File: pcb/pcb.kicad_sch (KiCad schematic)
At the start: 30 parts, among them J1 Barrel_Jack_Switch, Q1 RQ5P010SN, SW1 SW_SPST, SW2 SW_SPST, SW3 SW_SPST, U1 L7805, U2 MCP1406/07, U3 MCP7940N-xSN, U4 Pico, Y1 Crystal

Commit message: finished routing
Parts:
- removed Y1: Crystal, vfd:Crystal_DS26_D2.0mm_L6.0mm_Horizontal_SMT, symbol Device:Crystal
- added C10, C9: 0.1uF, Capacitor_SMD:C_1206_3216Metric_Pad1.33x1.80mm_HandSolder, symbol Device:C
- added H1: MountingHole_Pad, MountingHole:MountingHole_3.2mm_M3_DIN965_Pad, symbol Mechanical:MountingHole_Pad
- added J2: Conn_01x05_Pin, Connector_PinHeader_2.54mm:PinHeader_1x05_P2.54mm_Vertical, symbol Connector:Conn_01x05_Pin
- added J3: Conn_01x03_Pin, Connector_PinHeader_2.54mm:PinHeader_1x03_P2.54mm_Vertical, symbol Connector:Conn_01x03_Pin
- added J4: Conn_01x05_Pin, Connector_PinHeader_2.54mm:PinHeader_1x05_P2.54mm_Horizontal, symbol Connector:Conn_01x05_Pin
- added J5: Conn_01x03_Pin, Connector_PinHeader_2.54mm:PinHeader_1x03_P2.54mm_Horizontal, symbol Connector:Conn_01x03_Pin
- added R2: 22, Resistor_SMD:R_1206_3216Metric_Pad1.30x1.75mm_HandSolder, symbol Device:R
- added TP1: HV, TestPoint:TestPoint_THTPad_D1.5mm_Drill0.7mm, symbol Connector:TestPoint
- added TP2: 12V, TestPoint:TestPoint_THTPad_D1.5mm_Drill0.7mm, symbol Connector:TestPoint
- added TP3, TP6: 5V, TestPoint:TestPoint_THTPad_D1.5mm_Drill0.7mm, symbol Connector:TestPoint
- added TP4, TP8: GND, TestPoint:TestPoint_THTPad_D1.5mm_Drill0.7mm, symbol Connector:TestPoint
- added TP5, TP7: 3.3V, TestPoint:TestPoint_THTPad_D1.5mm_Drill0.7mm, symbol Connector:TestPoint
- added U3: MAX6921AWI, Package_SO:SOIC-28W_7.5x17.9mm_P1.27mm, symbol vfd:MAX6921AWI
- added V1: IV-18, vfd:IV-18, symbol vfd:IV-18
- added Y1: Crystal_GND3, vfd:Crystal_DS26_D2.0mm_L6.0mm_Horizontal_Grounded_SMT, symbol Device:Crystal_GND3
- renumbered C9 to C11, C10 to C12, C11 to C13, R2 to R3, R3 to R4, R4 to R5, U3 to U4, U4 to U5
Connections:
- net +12V: now also TP2.1
- net +3.3V: now also C9.2, J3.1 (Pin_1), TP5.1, U3.28 (VCC); no longer C11.1, R3.1, R4.1, R5.1, U4.8 (VCC), U5.36 (3V3)
- net +5V: now also J3.3 (Pin_3), R2.1, TP3.1; no longer D3.2 (A)
- net 30-50V: now also C10.1, TP1.1, U3.1 (VBB)
- net BOOST: now also J2.5 (Pin_5)
- net GND: now also C10.2, C9.1, H1.1, J3.2 (Pin_2), TP4.1, U3.14 (GND), V1.13 (Fil); no longer BT1.2 (-), C11.2, C12.2, C13.2, SW1.2 (B), SW2.2 (B), SW3.2 (B), U4.4 (VSS), U5.13 (GND), U5.18 (GND), U5.23 (GND), U5.28 (GND), U5.3 (GND), U5.38 (GND), U5.42 (GND), U5.8 (GND)
- net MFP: now also U5.25 (GPIO19)
- net SCL: now also U5.26 (GPIO20)
- net SDA: now also U5.27 (GPIO21)
- net SWITCH1: now also U5.31 (GPIO26_ADC0)
- net SWITCH2: now also U5.32 (GPIO27_ADC1)
- net SWITCH3: now also U5.34 (GPIO28_ADC2)
- net at C13.1, U4.2 (X2): now also Y1.2
- net GATE: now reaches C8.1, Q1.1 (G), U2.6 (~{OUT}), U2.7 (~{OUT})
- net at C12.1, U4.1 (X1): now also Y1.1
- net MCU_DATA: now reaches U5.10 (GPIO7)
- net MCU_DATA: now also J4.3 (Pin_3)
- net MCU_LATCH: now reaches U5.11 (GPIO8)
- net MCU_LATCH: now also J4.2 (Pin_2)
- net MCU_BLANK: now reaches U5.12 (GPIO9)
- net MCU_BLANK: now also J4.1 (Pin_1)
- net MCU_BOOST: now reaches U5.29 (GPIO22)
- net MCU_BOOST: now also J4.5 (Pin_5)
- net MCU_CLOCK: now reaches U5.9 (GPIO6)
- net MCU_CLOCK: now also J4.4 (Pin_4)
- new net: U3.10 (OUT12), V1.11 (F)
- new net: U3.11 (OUT11), V1.10 (B)
- new net: U3.12 (OUT10), V1.9 (G)
- new net: U3.17 (OUT9), V1.12 (A)
- new net: U3.18 (OUT8), V1.14 (D9)
- new net: U3.19 (OUT7), V1.15 (D1)
- new net: U3.20 (OUT6), V1.16 (D3)
- new net: U3.21 (OUT5), V1.17 (D5)
- new net: U3.22 (OUT4), V1.18 (D8)
- new net: U3.23 (OUT3), V1.19 (D7)
- new net: U3.24 (OUT2), V1.20 (D6)
- new net: U3.25 (OUT1), V1.21 (D4)
- new net: U3.26 (OUT0), V1.22 (D2)
- new net: U3.6 (OUT16), V1.2 (DP)
- new net: U3.7 (OUT15), V1.3 (D)
- new net: U3.8 (OUT14), V1.4 (C)
- new net: U3.9 (OUT13), V1.5 (E)
- new net: R2.2, V1.1 (Fil)
- new net +3.3VA: C11.1, J5.3 (Pin_3), R3.1, R4.1, R5.1, TP7.1, U4.8 (VCC), U5.36 (3V3)
- new net +5VA: D3.2 (A), J5.1 (Pin_1), TP6.1
- new net BLANK: J2.1 (Pin_1), U3.13 (BLANK)
- new net CLOCK: J2.4 (Pin_4), U3.15 (CLK)
- new net DATA: J2.3 (Pin_3), U3.27 (DIN)
- new net GNDA: BT1.2 (-), C11.2, C12.2, C13.2, J5.2 (Pin_2), SW1.2 (B), SW2.2 (B), SW3.2 (B), TP8.1, U4.4 (VSS), U5.38 (GND), Y1.3
- new net LATCH: J2.2 (Pin_2), U3.16 (LOAD)
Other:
- note added: "VFD"
- moved on the sheet: BT1, C11, C12, C13, D3, R3, R4, R5, SW1, SW2, SW3, U4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

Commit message: finished pcb
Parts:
- removed J2: Conn_01x05_Pin, Connector_PinHeader_2.54mm:PinHeader_1x05_P2.54mm_Vertical, symbol Connector:Conn_01x05_Pin
- removed J4: Conn_01x05_Pin, Connector_PinHeader_2.54mm:PinHeader_1x05_P2.54mm_Horizontal, symbol Connector:Conn_01x05_Pin
- added J2: Conn_01x06_Pin, Connector_PinHeader_2.54mm:PinHeader_1x06_P2.54mm_Vertical, symbol Connector:Conn_01x06_Pin
- added J4: Conn_01x06_Pin, Connector_PinHeader_2.54mm:PinHeader_1x06_P2.54mm_Horizontal, symbol Connector:Conn_01x06_Pin
- added Q2: IRLML6244, Package_TO_SOT_SMD:SOT-23_Handsoldering, symbol vfd:IRLML6244
- added R3: 470, Resistor_SMD:R_1206_3216Metric_Pad1.30x1.75mm_HandSolder, symbol Device:R
- renumbered R3 to R4, R4 to R5, R5 to R6
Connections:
- net BLANK: now also J2.1 (Pin_1)
- net BOOST: now also J2.5 (Pin_5)
- net CLOCK: now also J2.4 (Pin_4)
- net DATA: now also J2.3 (Pin_3)
- net GND: now also Q2.2 (S); no longer V1.13 (Fil)
- net LATCH: now also J2.2 (Pin_2)
- net MCU_BLANK: now also J4.1 (Pin_1)
- net MCU_BOOST: now also J4.5 (Pin_5)
- net MCU_CLOCK: now also J4.4 (Pin_4)
- net MCU_DATA: now also J4.3 (Pin_3)
- net MCU_LATCH: now also J4.2 (Pin_2)
- net F: now reaches U3.10 (OUT12), V1.11 (F)
- net B: now reaches U3.11 (OUT11), V1.10 (B)
- net G: now reaches U3.12 (OUT10), V1.9 (G)
- net A: now reaches U3.17 (OUT9), V1.12 (A)
- net D9: now reaches U3.18 (OUT8), V1.14 (D9)
- net D1: now reaches U3.19 (OUT7), V1.15 (D1)
- net D3: now reaches U3.20 (OUT6), V1.16 (D3)
- net D5: now reaches U3.21 (OUT5), V1.17 (D5)
- net D8: now reaches U3.22 (OUT4), V1.18 (D8)
- net D7: now reaches U3.23 (OUT3), V1.19 (D7)
- net D6: now reaches U3.24 (OUT2), V1.20 (D6)
- net D4: now reaches U3.25 (OUT1), V1.21 (D4)
- net D2: now reaches U3.26 (OUT0), V1.22 (D2)
- net DP: now reaches U3.6 (OUT16), V1.2 (DP)
- net D: now reaches U3.7 (OUT15), V1.3 (D)
- net C: now reaches U3.8 (OUT14), V1.4 (C)
- net E: now reaches U3.9 (OUT13), V1.5 (E)
- net MCU_FIL: now reaches U5.24 (GPIO18)
- net MCU_FIL: now also J4.6 (Pin_6)
- new net: Q2.1 (G), R3.2
- new net: Q2.3 (D), V1.13 (Fil)
- new net FIL: J2.6 (Pin_6), R3.1
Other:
- moved on the sheet: J3

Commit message: finished pcb
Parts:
- BT1: value Battery_Cell -> CR2032
- R1: value 10k -> 100k
- Y1: value Crystal_GND3 -> 32.768KHZ
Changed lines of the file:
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@@
       (effects (font (size 1.27 1.27)) (justify left))
     )
-    (property "Value" "Crystal_GND3" (at 167.64 229.87 90)
+    (property "Value" "32.768KHZ" (at 182.88 231.14 90)
       (effects (font (size 1.27 1.27)) (justify left))
     )
@@
       (effects (font (size 1.27 1.27)) (justify left))
     )
-    (property "Value" "10k" (at 90.17 50.8 0)
+    (property "Value" "100k" (at 88.9 50.8 0)
       (effects (font (size 1.27 1.27)) (justify left))
     )
@@
       (effects (font (size 1.27 1.27)) (justify left))
     )
-    (property "Value" "Battery_Cell" (at 210.82 220.4085 0)
-      (effects (font (size 1.27 1.27)) (justify left))
-    )
+    (property "Value" "CR2032" (at 210.82 220.4085 0)
+      (effects (font (size 1.27 1.27)) (justify left))
+    )

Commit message: new pcb design
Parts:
- removed J2: Conn_01x06_Pin, Connector_PinHeader_2.54mm:PinHeader_1x06_P2.54mm_Vertical, symbol Connector:Conn_01x06_Pin
- removed J3: Conn_01x03_Pin, Connector_PinHeader_2.54mm:PinHeader_1x03_P2.54mm_Vertical, symbol Connector:Conn_01x03_Pin
- removed J4: Conn_01x06_Pin, Connector_PinHeader_2.54mm:PinHeader_1x06_P2.54mm_Horizontal, symbol Connector:Conn_01x06_Pin
- removed J5: Conn_01x03_Pin, Connector_PinHeader_2.54mm:PinHeader_1x03_P2.54mm_Horizontal, symbol Connector:Conn_01x03_Pin
- added J2, J3: Conn_02x05_Odd_Even, Connector_PinSocket_2.54mm:PinSocket_2x05_P2.54mm_Vertical, symbol Connector_Generic:Conn_02x05_Odd_Even
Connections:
- net +3.3V: now also J2.1 (Pin_1)
- net +3.3VA: now also J3.1 (Pin_1)
- net +5V: now also J2.3 (Pin_3)
- net +5VA: now also J3.3 (Pin_3)
- net BLANK: now also J2.8 (Pin_8)
- net BOOST: now also J2.9 (Pin_9)
- net CLOCK: now also J2.2 (Pin_2)
- net DATA: now also J2.4 (Pin_4)
- net FIL: now also J2.10 (Pin_10)
- net GND: now also J2.5 (Pin_5)
- net GNDA: now also J3.5 (Pin_5)
- net LATCH: now also J2.6 (Pin_6)
- net MCU_BLANK: now also J3.8 (Pin_8)
- net MCU_BOOST: now also U5.22 (GPIO17), J3.9 (Pin_9); no longer U5.29 (GPIO22)
- net MCU_CLOCK: now also J3.2 (Pin_2)
- net MCU_DATA: now also J3.4 (Pin_4)
- net MCU_FIL: now also J3.10 (Pin_10)
- net MCU_LATCH: now also J3.6 (Pin_6)

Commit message: small fixes
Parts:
- removed D2: SDT5A60SA-13, Diode_SMD:D_SMA_Handsoldering, symbol Device:D_Schottky
- added D2: FM4004-W, Diode_SMD:D_SMA_Handsoldering, symbol Device:D
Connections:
- net +12V: now also D2.2 (A)
- net at C6.1, U1.1 (IN): now also D2.1 (K)

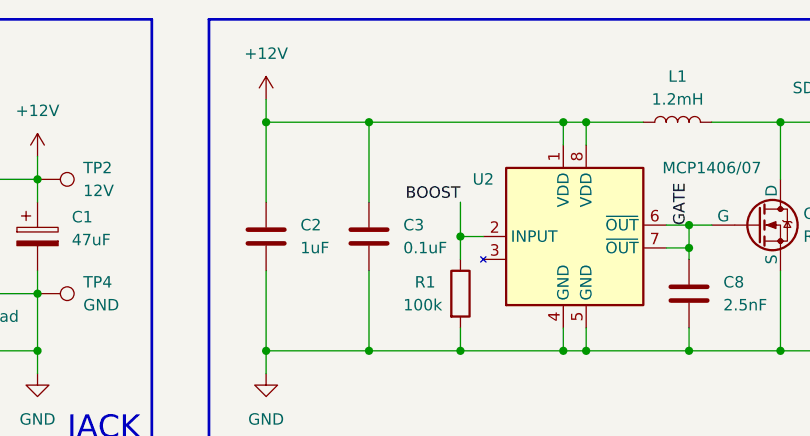
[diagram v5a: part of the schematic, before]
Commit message: added info for boost converter signal
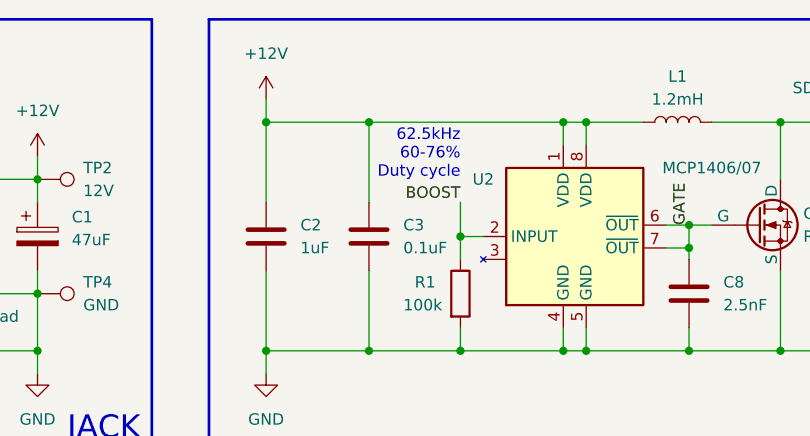
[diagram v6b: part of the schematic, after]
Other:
- note added: "62.5kHz 60-76% Duty cycle"
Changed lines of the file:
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@@
     (effects (font (size 2.54 2.54)) (justify right bottom))
+  )
+  (text "62.5kHz\n60-76%\nDuty cycle" (at 95.25 36.83 0)
+    (effects (font (size 1.27 1.27)) (justify right bottom))
   )
   (text "JACK" (at 59.69 66.04 0)

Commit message: added shift register code
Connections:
- net SCL: now also U5.27 (GPIO21); no longer U5.26 (GPIO20)
- net SDA: now also U5.26 (GPIO20); no longer U5.27 (GPIO21)
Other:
- note added: "reversed in R1.0"
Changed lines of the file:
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@@
     (effects (font (size 1.27 1.27)) (justify right bottom))
+  )
+  (text "reversed\nin R1.0" (at 83.82 245.11 0)
+    (effects (font (size 1.27 1.27)) (justify left bottom))
   )
   (text "JACK" (at 59.69 66.04 0)
@@
     (effects (font (size 1.27 1.27)) (justify right bottom))
   )
-  (label "SCL" (at 82.55 245.11 180) (fields_autoplaced)
+  (label "SDA" (at 82.55 245.11 180) (fields_autoplaced)
     (effects (font (size 1.27 1.27)) (justify right bottom))
   )
@@
     (effects (font (size 1.27 1.27)) (justify right bottom))
   )
-  (label "SDA" (at 82.55 242.57 180) (fields_autoplaced)
-    (effects (font (size 1.27 1.27)) (justify right bottom))
-  )
+  (label "SCL" (at 82.55 242.57 180) (fields_autoplaced)
+    (effects (font (size 1.27 1.27)) (justify right bottom))
+  )

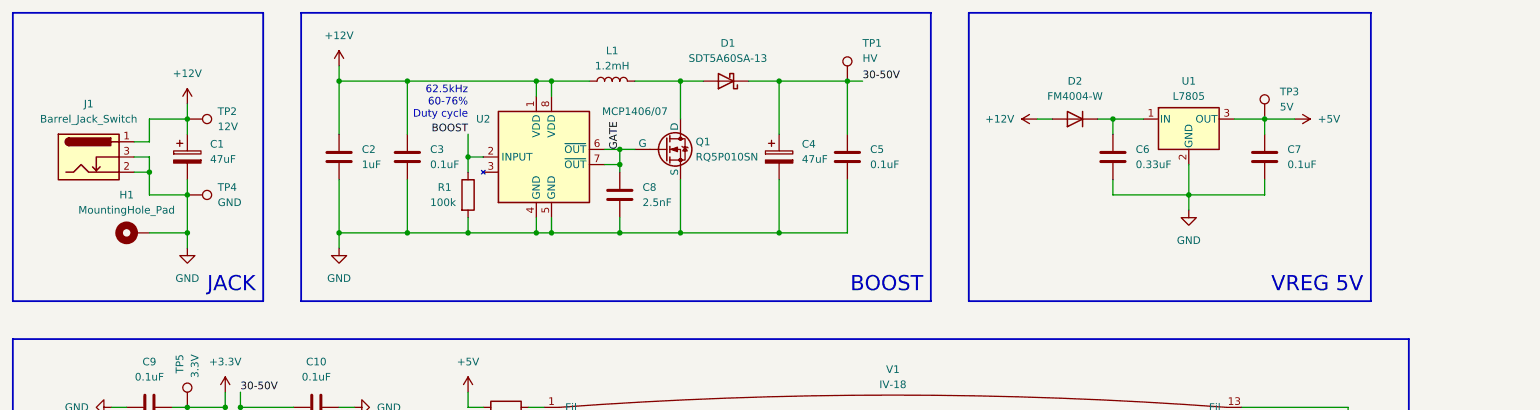
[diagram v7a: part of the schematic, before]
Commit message: added resettable fuse
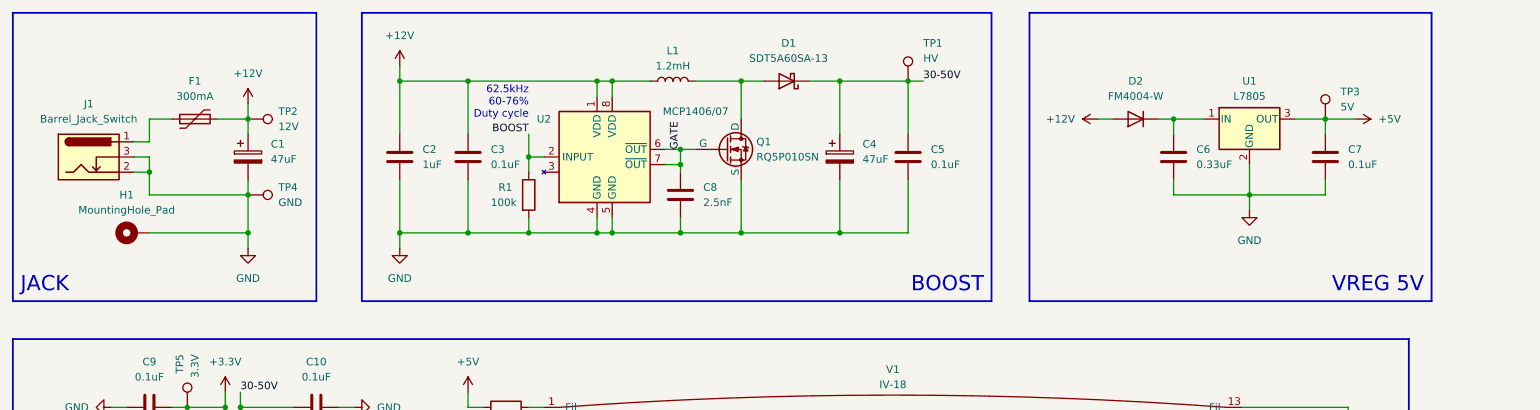
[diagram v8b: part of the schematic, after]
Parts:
- added F1: 300mA, Fuse:Fuse_1812_4532Metric_Pad1.30x3.40mm_HandSolder, symbol Device:Polyfuse
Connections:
- net +12V: now also F1.2; no longer J1.1
- new net: F1.1, J1.1
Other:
- moved on the sheet: C1, C2, C3, C4, C5, C6, C7, C8, D1, D2, L1, Q1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
